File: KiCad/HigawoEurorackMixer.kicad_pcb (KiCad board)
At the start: 2 copper layers, 68.1 x 128.5 mm, 23 parts, among them J1 AudioJack2_SwitchT, J2 AudioJack2_SwitchT, J3 AudioJack2_SwitchT, J4 AudioJack2_SwitchT, J5 AudioJack2_SwitchT, J6 EURO_PWR_2x5, U2 TL072

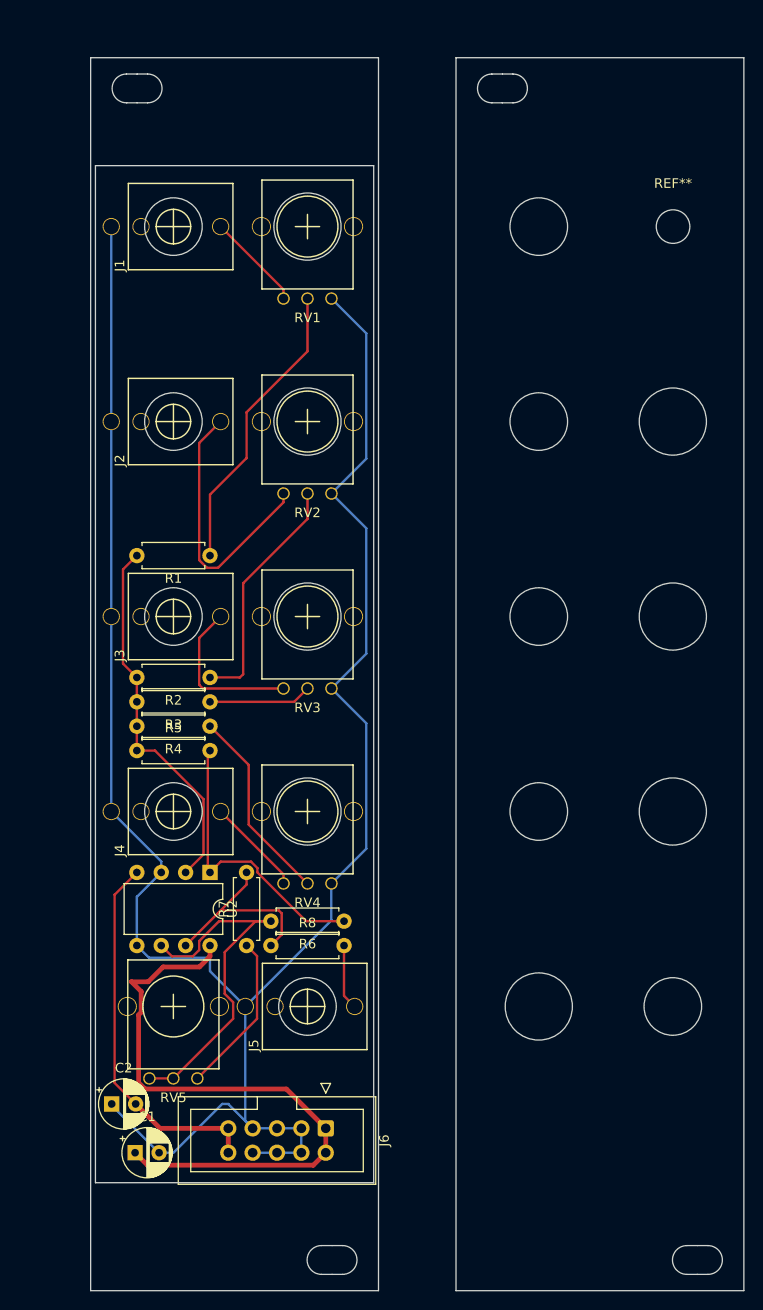
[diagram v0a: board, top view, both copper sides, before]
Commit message: main board needs mirroring
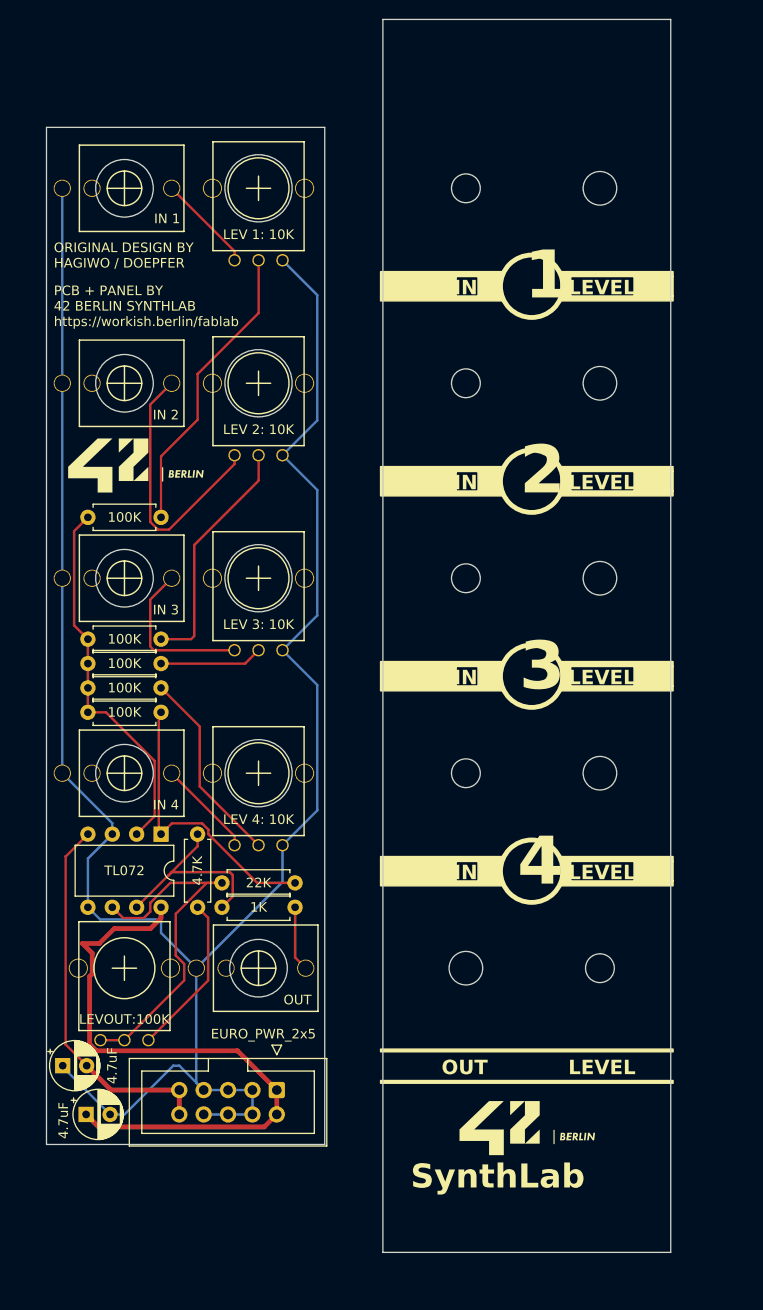
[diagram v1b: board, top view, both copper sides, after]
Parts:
- added REF**: IN 1, MountingHole:MountingHole_3.5mm, F.Cu at (129.5, 114.1)
- added REF**: Eurorack_Panel_ScrewHole_Oval, Library:Eurorack_Panel_ScrewHole_Oval, F.Cu at (132.1, 161.1)
- added REF**: MountingHole_3mm, MountingHole:MountingHole_3mm, F.Cu at (115.6, 114.1)
- added REF**: IN 1, MountingHole:MountingHole_3.5mm, F.Cu at (129.5, 93.8)
- added REF**: IN 1, MountingHole:MountingHole_3.5mm, F.Cu at (115.6, 134.4)
- added REF**: MountingHole_3mm, MountingHole:MountingHole_3mm, F.Cu at (115.6, 73.5)
- added REF**: MountingHole_3mm, MountingHole:MountingHole_3mm, F.Cu at (115.6, 53.2)
- added REF**: MountingHole_3mm, MountingHole:MountingHole_3mm, F.Cu at (129.5, 134.4)
- added REF**: Eurorack_Panel_ScrewHole_Oval, Library:Eurorack_Panel_ScrewHole_Oval, F.Cu at (111.8, 38.6)
- added REF**: MountingHole_3mm, MountingHole:MountingHole_3mm, F.Cu at (115.6, 93.8)
- added REF**: IN 1, MountingHole:MountingHole_3.5mm, F.Cu at (129.5, 73.5)
- J1: value AudioJack2_SwitchT -> IN 1
- J2: value AudioJack2_SwitchT -> IN 2
- J3: value AudioJack2_SwitchT -> IN 3
- J4: value AudioJack2_SwitchT -> IN 4
- J5: value AudioJack2_SwitchT -> OUT
- RV1: value 10K -> LEV 1: 10K
- RV2: value 10K -> LEV 2: 10K
- RV3: value 10K -> LEV 3: 10K
- RV4: value 10K -> LEV 4: 10K
- RV5: value 100K -> LEVOUT:100K
- moved REF** 8.60 mm to (129.5, 53.2)
- moved C2 6.48 mm to (73.6, 144.6)
- moved J3 6.48 mm to (80.0, 93.8)
- moved J5 6.48 mm to (94.0, 134.4)
- moved J6 6.48 mm to (95.9, 147.1)
- moved R3 6.48 mm to (83.8, 102.7)
- moved R5 6.48 mm to (76.2, 107.8)
- moved R8 6.48 mm to (90.1, 128.1)
- moved RV3 6.48 mm to (94.0, 93.8)
- moved RV5 6.48 mm to (80.0, 134.4)
- moved J1 6.48 mm to (80.0, 53.2)
- moved RV1 6.48 mm to (94.0, 53.2)
- moved J2 6.48 mm to (80.0, 73.5)
- moved J4 6.48 mm to (80.0, 114.1)
- moved R1 6.48 mm to (83.8, 87.5)
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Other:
- board size 68.1 x 128.5 mm -> 65.1 x 128.5 mm
- board text added: "1"
- board text added: "2"
- board text added: "3"
- board text added: "4"
- board text added: "IN"
- board text added: "LEVEL"
- board text added: "ORIGINAL DESIGN BY HAGIWO / DOEPFER"
- board text added: "PCB + PANEL BY 42 BERLIN SYNTHLAB https://workish.berlin/fablab"
- board text removed: "IN 1"
- board text removed: "IN 2"
- board text removed: "IN 3"
- board text removed: "IN 4"

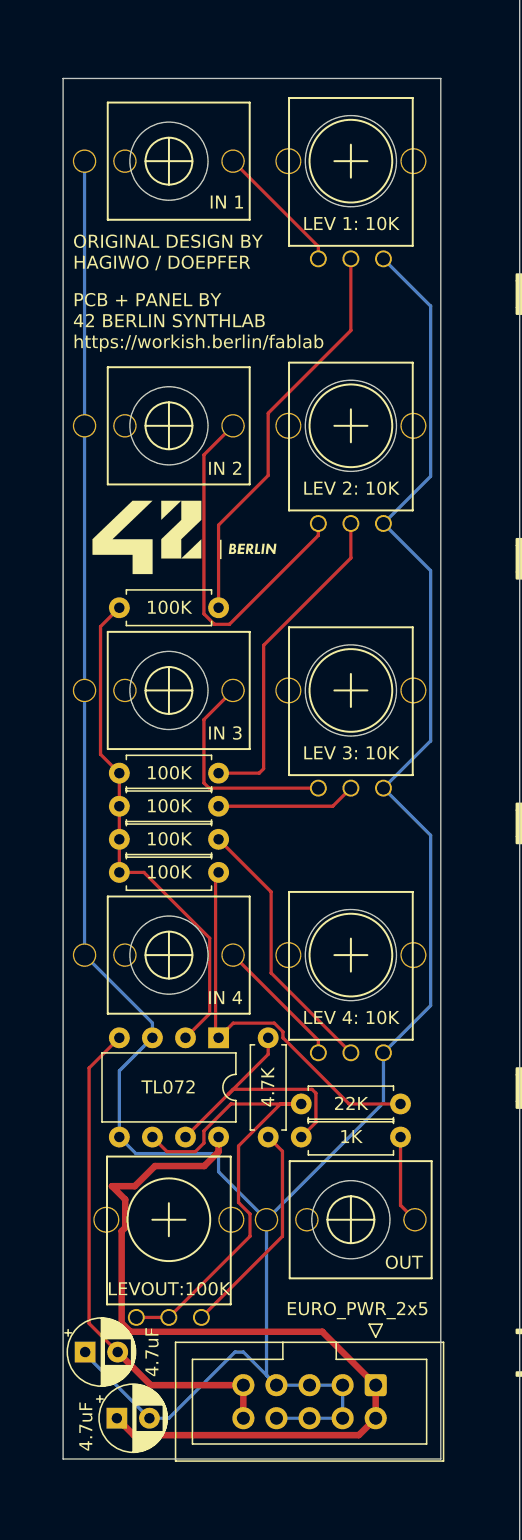
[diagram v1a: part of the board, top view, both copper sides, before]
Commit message: mirrored version of PCB completed
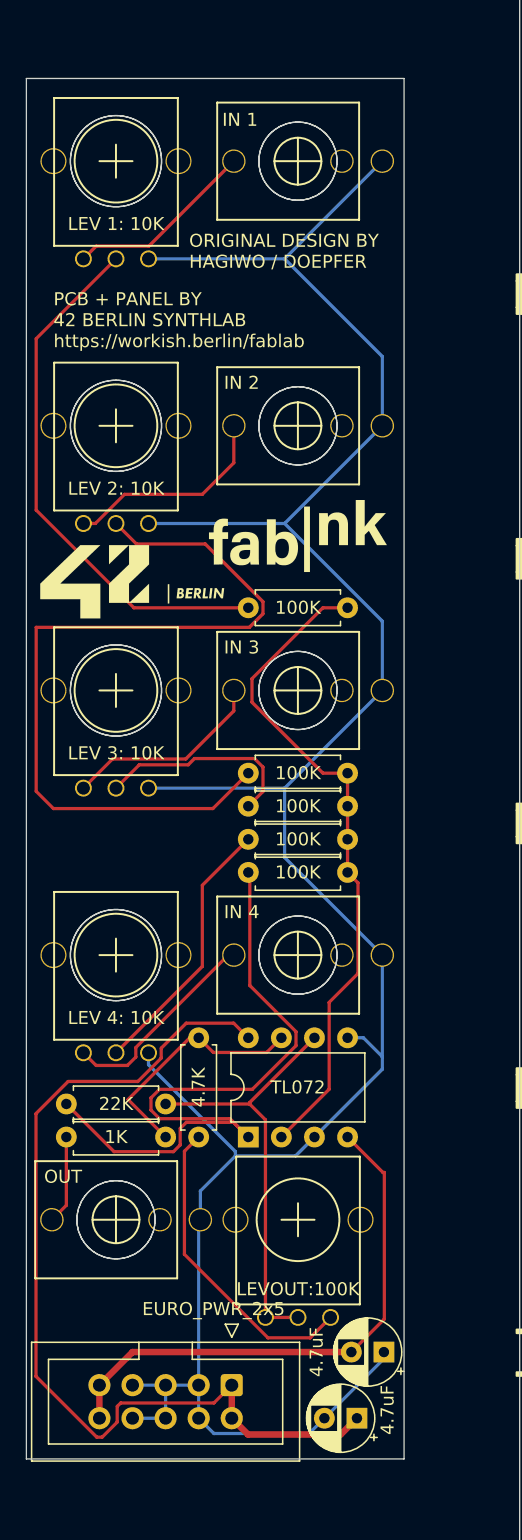
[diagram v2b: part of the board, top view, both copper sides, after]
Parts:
- moved R6 25.7 mm to (72.1, 125.5), turned to 0 degrees
- moved C2 22.9 mm to (96.5, 144.6), turned to 180 degrees
- moved C1 18.4 mm to (94.4, 149.7), turned to 180 degrees
- moved J5 18.0 mm to (75.9, 134.4), turned to 90 degrees
- moved RV1 18.0 mm to (75.9, 53.2)
- moved RV2 18.0 mm to (75.9, 73.5)
- moved RV3 18.0 mm to (75.9, 93.8)
- moved RV4 18.0 mm to (75.9, 114.1)
- moved R5 17.5 mm to (93.7, 107.8), turned to 180 degrees
- moved J6 11.1 mm to (84.8, 147.1)
- moved R8 10.4 mm to (79.7, 128.1), turned to 180 degrees
- moved RV5 9.92 mm to (89.9, 134.4)
- moved J1 9.90 mm to (89.9, 53.2), turned to 90 degrees
- moved J2 9.90 mm to (89.9, 73.5), turned to 90 degrees
- moved J3 9.90 mm to (89.9, 93.8), turned to 90 degrees
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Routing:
- net Net-(R2-Pad1): track 25.2 -> 63.1 mm
- net GND: track 225.2 -> 196.8 mm
- net Net-(R5-Pad2): track 30.2 -> 54.5 mm
- net Net-(U2A--): track 39.0 -> 51.7 mm
- net Net-(J2-PadT): track 28.2 -> 16.3 mm
- net Net-(R1-Pad1): track 31.0 -> 41.2 mm
- net Net-(R7-Pad1): track 16.9 -> 24.0 mm
- net Net-(U2C-V+): track 66.7 -> 72.8 mm
- net Net-(U2B--): track 38.7 -> 33.0 mm
- net Net-(J4-PadT): track 10.2 -> 15.9 mm
- net Net-(R3-Pad1): track 10.7 -> 16.0 mm
- net Net-(J1-PadT): track 10.2 -> 14.7 mm
- net Net-(U2C-V-): track 39.2 -> 41.7 mm
- net Net-(R7-Pad2): track 21.1 -> 18.7 mm
- net Net-(J3-PadT): track 17.0 -> 15.6 mm
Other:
- board size 65.1 x 128.5 mm -> 67.9 x 128.5 mm
